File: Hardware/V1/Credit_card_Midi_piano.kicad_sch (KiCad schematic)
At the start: 1 part

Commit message: motherboard update
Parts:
- added J3, J4: 0, Resistor_SMD:R_0603_1608Metric, symbol Device:R_Small
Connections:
- new net Audio_out/VCC_Audio: J3.1, J4.2
- new net Controller/3V3: J4.1
- new net Controller/VBUS: J3.2
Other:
- sheet Audio_out ports: added ADC_Micro, Audio_left, Audio_right, Buzzer, VCC_Audio; removed none
- sheet Controller ports: added 3V3, A1, A2, A3, GIO21, GIO24, GIO25, GIO26, GPIO0, GPIO1, VBUS; removed none

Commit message: added keys
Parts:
- removed RN1: CAT10-103J4LF, CAT10J4LF, symbol SamacSys_Parts:CAT10-103J4LF
- added H1: Ground_Pen, MountingHole:MountingHole_3.2mm_M3_Pad_Via, symbol Mechanical:MountingHole_Pad
- added H2: VCC_PEN, MountingHole:MountingHole_3.2mm_M3_Pad_Via, symbol Mechanical:MountingHole_Pad
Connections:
- net GND: now also H1.1
- net Audio_out/VCC_Audio renamed VCC_AUDIO
- net Controller/3V3 renamed 3V3
- net 3V3: now also H2.1
- net Controller/VBUS renamed VUSB

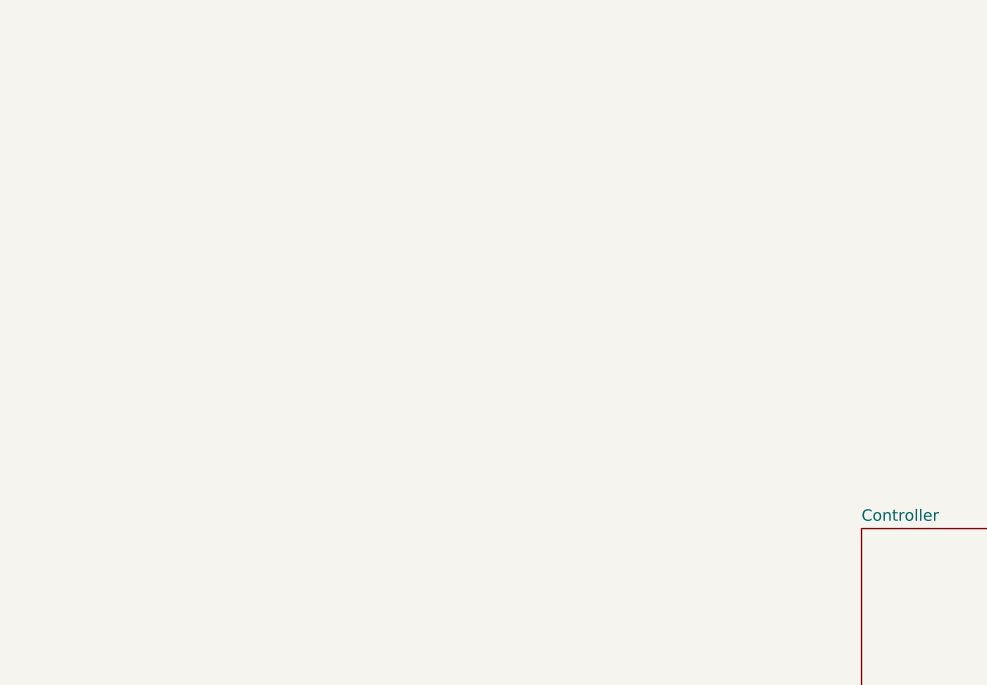
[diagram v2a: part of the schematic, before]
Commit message: refined footprint
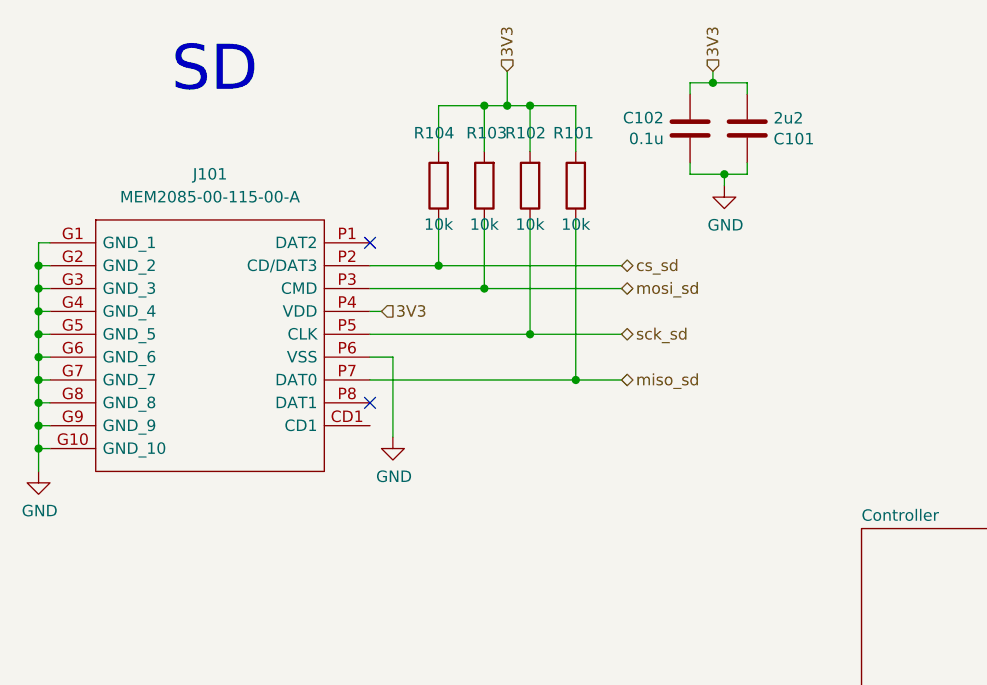
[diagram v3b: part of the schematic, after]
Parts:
- added C101: 2u2, Capacitor_SMD:C_0805_2012Metric_Pad1.18x1.45mm_HandSolder, symbol SymbolsBalloonv4:C
- added C102: 0.1u, Capacitor_SMD:C_0402_1005Metric_Pad0.74x0.62mm_HandSolder, symbol SymbolsBalloonv4:C
- added J101: MEM2085-00-115-00-A, SamacSys_Parts:MEM20850011500A, symbol SamacSys_Parts:MEM2085-00-115-00-A
- added R101, R102, R103, R104: 10k, Resistor_SMD:R_0603_1608Metric_Pad0.98x0.95mm_HandSolder, symbol SymbolsBalloonv4:R
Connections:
- net 3V3: now also C101.2, C102.1, J101.P4 (VDD), R101.2, R102.2, R103.2, R104.2
- net GND: now also C101.1, C102.2, J101.G1 (GND_1), J101.G10 (GND_10), J101.G2 (GND_2), J101.G3 (GND_3), J101.G4 (GND_4), J101.G5 (GND_5), J101.G6 (GND_6), J101.G7 (GND_7), J101.G8 (GND_8), J101.G9 (GND_9), J101.P6 (VSS)
- new net cs_sd: J101.P2 (CD/DAT3), R104.1
- new net miso_sd: J101.P7 (DAT0), R101.1
- new net mosi_sd: J101.P3 (CMD), R103.1
- new net sck_sd: J101.P5 (CLK), R102.1
- no-connect marks 0 -> 2
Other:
- note added: "SD"

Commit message: a
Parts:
- removed C101: 2u2, Capacitor_SMD:C_0805_2012Metric_Pad1.18x1.45mm_HandSolder, symbol SymbolsBalloonv4:C
- removed C102: 0.1u, Capacitor_SMD:C_0402_1005Metric_Pad0.74x0.62mm_HandSolder, symbol SymbolsBalloonv4:C
- removed J101: MEM2085-00-115-00-A, SamacSys_Parts:MEM20850011500A, symbol SamacSys_Parts:MEM2085-00-115-00-A
- removed R101, R102, R103, R104: 10k, Resistor_SMD:R_0603_1608Metric_Pad0.98x0.95mm_HandSolder, symbol SymbolsBalloonv4:R
- added J101: 502352-0200, 5023520200, symbol SamacSys_Parts:502352-0200
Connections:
- no-connect marks 2 -> 0
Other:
- added sheet SD (SD.kicad_sch)
- sheet Controller ports: added SPI_CS, SPI_MISO, SPI_MOSI, SPI_SCK; removed none
- note removed: "SD"

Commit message: asd
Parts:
- removed H1: Ground_Pen, MountingHole:MountingHole_3.2mm_M3_Pad_Via, symbol Mechanical:MountingHole_Pad
- removed H2: VCC_PEN, MountingHole:MountingHole_3.2mm_M3_Pad_Via, symbol Mechanical:MountingHole_Pad
- removed J3, J4: 0, Resistor_SMD:R_0603_1608Metric, symbol Device:R_Small
- PEN_CON1: renamed from J101; footprint 5023520200 -> SamacSys_Parts:5023520200
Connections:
- net 3V3: now also PEN_CON1.1
- net GND: now also PEN_CON1.2
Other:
- sheet Audio_out ports: added 3V3_D, Audio_0, Audio_1, Audio_2; removed ADC_Micro, Audio_left, Audio_right
- sheet Controller ports: added GPIO22, GPIO23, GPIO28, GPIO29, VSYS; removed A1, A2, A3, GIO21, GIO24, GIO25, GIO26, GPIO0, GPIO1, VBUS
- moved on the sheet: PEN_CON1

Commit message: wirked on iS2
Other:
- sheet Audio_out ports: added Audio_BCK, Audio_DIN, Audio_LRC; removed Audio_0, Audio_1, Audio_2
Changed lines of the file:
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@@
 (kicad_sch
-	(version 20231120)
+	(version 20250114)
 	(generator "eeschema")
-	(generator_version "8.0")
+	(generator_version "9.0")
 	(paper "A4")
+	(text_box "Known Issues\n- Battery Controller shuts down when there's no battery,\nso operation with only USB is impossible. \nBC can be shunted to bypass that\n- Audio Jack not enough on the edge, aux needs to be modified\n- USBC could be more on the edge as well\n- LDOs not Bucks\n- Layout could be refined\n- uSD covers Logo"
+		(exclude_from_sim no)
+		(at 199.39 119.38 0)
+		(size 68.58 19.05)
+		(margins 0.9525 0.9525 0.9525 0.9525)
+		(stroke
+			(width 0)
+			(type solid)
+		)
+		(fill
+			(type none)
+		)
+		(effects
+			(font
+				(size 1.27 1.27)
+			)
+			(justify left top)
+		)
+	)
 	(junction
 		(at 172.72 88.8851)
@@
 	(label "3V3"
 		(at 203.2 55.88 180)
-		(fields_autoplaced yes)
 		(effects
 			(font
@@
 	(label "3V3"
 		(at 107.95 88.9 0)
-		(fields_autoplaced yes)
 		(effects
 			(font
@@
 	(label "V_SYS"
 		(at 172.72 88.9 0)
-		(fields_autoplaced yes)
 		(effects
 			(font
@@
 		(at 123.19 86.36)
 		(size 33.02 17.145)
+		(exclude_from_sim no)
+		(in_bom yes)
+		(on_board yes)
+		(dnp no)
 		(fields_autoplaced yes)
 		(stroke
@@
 		(at 67.945 85.09)
 		(size 13.335 17.145)
+		(exclude_from_sim no)
+		(in_bom yes)
+		(on_board yes)
+		(dnp no)
 		(fields_autoplaced yes)
 		(stroke
@@
 		(at 196.85 86.36)
 		(size 17.145 17.145)
+		(exclude_from_sim no)
+		(in_bom yes)
+		(on_board yes)
+		(dnp no)
 		(fields_autoplaced yes)
 		(stroke
@@
 			)
 		)
-		(pin "Audio_0" input
-			(at 196.85 92.71 180)
-			(effects
-				(font
-					(size 1.27 1.27)
-				)
-				(justify left)
-			)
-		)
-		(pin "Audio_1" input
-			(at 196.85 95.25 180)
-			(effects
-				(font
-					(size 1.27 1.27)
-				)
-				(justify left)
-			)
-		)
 		(pin "3V3_D" input
 			(at 210.82 86.36 90)
@@
 			)
 		)
-		(pin "Audio_2" input
-			(at 196.85 97.79 180)
-			(effects
-				(font
-					(size 1.27 1.27)
-				)
-				(justify left)
-			)
-		)
 		(pin "VCC_Audio" input
 			(at 196.85 88.9 180)
+			(effects
+				(font
+					(size 1.27 1.27)
+				)
+				(justify left)
+			)
+		)
+		(pin "Audio_BCK" input
+			(at 196.85 97.79 180)
+			(effects
+				(font
+					(size 1.27 1.27)
+				)
+				(justify left)
+			)
+		)
+		(pin "Audio_DIN" input
+			(at 196.85 95.25 180)
+			(effects
+				(font
+					(size 1.27 1.27)
+				)
+				(justify left)
+			)
+		)
+		(pin "Audio_LRC" input
+			(at 196.85 92.71 180)
 			(effects
 				(font
@@
 		)
 	)
+	(embedded_fonts no)
 )
